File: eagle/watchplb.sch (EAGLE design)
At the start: 141 parts, among them IC1 SAM-M8Q, IC2 BM70BLES1FC2-0B03AA, Q1 8MHz / LFXTAL020423Reel, Q2 BC817-25SMD, Q3 DMN3023L-7, Q4 16MHz_LFXTAL051370Reel, U1 MCP111-XXXXX/TO, U2 STM32L073RZ, U3 MCP2200-I/SS, U4 TPD3E001DRLR

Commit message: added rf amp and sma connector, reorganised for better pdf page ordering
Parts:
- added U$2: RA07H4047M, Hick:RA07H4047M
- added X1: (no value), adafruit:SMACONNECTOR_EDGE
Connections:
- removed net N$38: C24.2, U$1.VDD_IO
- new net +12V: U$2.DRAIN_VOLTAGE
- new net RF_SIGNAL_AMPLIFIED: U$2.RF_OUT, X1.ANT
- net +3V3: now also C24.2, U$1.VDD_IO, U$2.GATE_VOLTAGE
- net GND: now also U$2.RF_GND_L, U$2.RF_GND_R, X1.GND1, X1.GND2, X1.GND3, X1.GND4
- net RF_SIGNAL: now also U$2.RF_IN
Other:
- moved on the sheet: 3V3, BTN_1, BTN_2, BTN_3, BTN_4, BTN_NRST, BT_RX, BT_TX, C1, C10, C11, C12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

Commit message: added battery protection circuit
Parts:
- added BAT: (no value), pinhead:PINHD-1X5
- added C38, C39, C40, C41, C44, C45, C46: 100nF, resistor:C-EUC0805
- added C42, C43: 1uF, resistor:C-EUC0805
- added D6: Zener 16V MMSZ5246BS-7-F, diode-1:DIODE-SOD323-R
- added D7: 100V, BAS16J,135, diode-1:DIODE-SOD323-R
- added D8, D9: (no value), adafruit:DIODESOD-123
- added IC3: LM1117DTX-ADJ-12V, lm1117:LM1117DTX-ADJ
- added IC4: LM1117DTX-ADJ-3V3, lm1117:LM1117DTX-ADJ
- added Q5, Q6: CSD18534Q5A, CSD18534Q5A:CSD18534Q5A
- added R30, R31, R32, R33, R34: 1k, resistor:R-EU_M0805
- added R35: 10k, resistor:R-EU_M0805
- added R36: 20mR, resistor:R-EU_M0805
- added R37, R38: 100R, resistor:R-EU_M0805
- added R39: 10M, resistor:R-EU_M0805
- added R40, R43: 5k1, resistor:R-EU_M0805
- added R41: 3M3, resistor:R-EU_M0805
- added R42: 1M, resistor:R-EU_M0805
- added R44: 470k, resistor:R-EU_M0805
- added SPARE_WAKEUP, SPARE_WAKEUP1: PTR1B2,54, testpad:PTR1B2,54
- added TR1: NTC 103AT, discrete:THERMISTOR_R-7,5
- added U5: BQ7790504, chips:BQ77904
- R10, R11, R14, R15, R18, R19, R20, R21, R22: value 220R -> 470R
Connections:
- removed net V+: D1.C, JP2.1
- new net BAT_PACK_GND: BAT.5, C38.2, C39.2, C40.2, C41.2, C42.1, C43.2, C44.1, C46.2, R36.2, R37.2, TR1.1, U5.AVSS, U5.CTRC, U5.CTRD, U5.DVSS
- new net BAT_PACK_NEG: D6.A, Q6.1, Q6.2, Q6.3, R41.1, R44.2
- new net BAT_PACK_POS: BAT.1, R30.1, R34.1
- new net N$38: R35.2, TR1.2, U5.TS
- new net N$46: D6.C, D7.C, Q6.4, R41.2, R42.1
- new net N$47: BAT.2, R31.1
- new net N$48: BAT.3, R32.1
- new net N$49: BAT.4, R33.1
- new net N$50: C39.1, R33.2, U5.VC1
- new net N$51: C40.1, R32.2, U5.VC2
- new net N$52: C41.1, R31.2, U5.VC3
- new net N$53: C38.1, R30.2, U5.VC4, U5.VC5
- new net N$54: C43.1, R34.2, U5.VDD
- new net N$55: Q5.1, Q5.2, Q5.3, R36.1, R38.2, R39.2
- new net N$56: C42.2, U5.AVDD, U5.CCFG
- new net N$57: C45.2, C46.1, R38.1, U5.SRN
- new net N$58: C44.2, C45.1, R37.1, U5.SRP
- new net N$59: Q5.5, Q5.6, Q5.7, Q5.8, Q6.5, Q6.6, Q6.7, Q6.8
- new net N$60: R35.1, U5.VTB
- new net N$62: Q5.4, R39.1, R40.1
- new net N$63: R40.2, U5.DSG
- new net N$64: D7.A, R42.2, R43.2
- new net N$65: R43.1, U5.CHG
- new net N$66: R44.1, U5.LD
- new net N$67: D8.A, SPARE_WAKEUP1.TP
- new net N$68: D9.A, SPARE_WAKEUP.TP
- net +3V3: now also D1.C, JP2.1
- net MCU_WAKEUP: now also D8.C, D9.C

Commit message: added calculations as excel file and battery charge circuitry in schematic
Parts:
- removed X1: (no value), adafruit:SMACONNECTOR_EDGE
- added C47, C49: 100nF, resistor:C-EUC0805
- added C48, C51, C52: 22uF 80-EDK226M050A9GAA, rcl:CPOL-EUE
- added C50: 4.7uF, resistor:C-EUC0805
- added D10: MBRS330T3, diode:MBRS330T3
- added J3: BNCPTH, SparkFun-Connectors:BNCPTH
- added J4: (no value), SparkFun-Connectors:USB_MICRO-B_FEMALE-SMT
- added L8: CTX10-4A-R, CTX10-4A-R:CTX10-4A-R
- added Q7: DMN3023L-7, transistor-small-signal:BSS123
- added R45: 330, resistor:R-EU_M0805
- added R46: 910R, resistor:R-EU_M0805
- added R47, R49: 10k, resistor:R-EU_M0805
- added R48: 330k, resistor:R-EU_M0805
- added R50: 0.25R, resistor:R-EU_M0805
- added R51: 120k, resistor:R-EU_M0805
- added R52: 12k4, resistor:R-EU_M0805
- added U$3: LT1513, Hick:LT1513
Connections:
- removed net BAT_PACK_NEG: D6.A, Q6.1, Q6.2, Q6.3, R41.1, R44.2
- new net N$61: C50.2, L8.2, U$3.VSW
- new net N$69: C48.+, J4.VBUS, L8.1, U$3.VIN
- new net N$70: L8.3, R49.2, R50.2
- new net N$71: C47.2, R45.2
- new net N$72: R45.1, U$3.VC
- new net N$73: Q7.D, R46.1
- new net N$74: R46.2, R47.2, R48.1
- new net N$75: C50.1, D10.A, L8.4
- new net N$76: C49.2, R48.2, R49.1, U$3.IFB
- new net N$77: R51.1, R52.2, U$3.VFB
- new net S/S: U$3.S/S
- net +3V3: now also R47.1
- net BAT_PACK_POS: now also C51.+, C52.+, D10.C, R51.2
- net GND: now also C47.1, C48.-, C49.1, C51.-, C52.-, D6.A, J3.GND, J4.GND, J4.SHIELD, Q6.1, Q6.2, Q6.3, Q7.S, R41.1, R44.2, R50.1, R52.1, U$3.GND; no longer X1.GND1, X1.GND2, X1.GND3, X1.GND4
- net RF_SIGNAL_AMPLIFIED: now also J3.OUT; no longer X1.ANT
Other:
- note added: "kabel mouser nr 601-606BBP wird ebenfalls benötigt"
- moved on the sheet: IC3, IC4

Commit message: added linear regulators + calculations for them, exported parts as library, generated new pdf
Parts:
- removed IC4: LM1117DTX-ADJ-3V3, lm1117:LM1117DTX-ADJ
- added B1, B2, B3, B4, B5, B6, B7: BLM18KG601SN1D, PCB4_Demoboard:B-EU_B0603
- added C53, C56, C59: 10uF 80-EDK106M025A9DAA, rcl:CPOL-EUE
- added C54, C57, C60: 100uF 647-GYA1E101MCQ1GS, rcl:CPOL-EUE
- added C55, C58, C61: NP, rcl:CPOL-EUE
- added IC5: LM1117DTX-ADJ-10V, lm1117:LM1117DTX-ADJ
- added IC6: LM1117DTX-ADJ-3V3, lm1117:LM1117DTX-ADJ
- added JP3: Power Disconnect, pinhead:PINHD-1X2
- added R53, R55, R57: 5k1, resistor:R-EU_M0805
- added R54, R56, R58: 47k, resistor:R-EU_M0805
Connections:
- new net 10V_INTERMEDIATE: C57.+, C59.+, IC5.OUT, IC6.IN, R55.1
- new net N$78: B4.2, CONFIG_INTERFACE_TEST_POINT.2
- new net N$79: B2.2, C1.1, C2.1, C3.1, IC1.VCC, IC1.VCC_IO, IC1.V_BCKP, R1.1, R2.1
- new net N$80: B3.2, IC2.VBAT, LED1.A, R3.1, U1.VSS
- new net N$81: B5.2, D1.C, JP2.1
- new net N$82: B6.2, C24.2, U$1.VDD_IO
- new net N$83: B7.2, U$2.GATE_VOLTAGE
- new net N$84: C53.+, C56.+, IC3.IN, IC5.IN, JP3.2
- new net N$85: C55.+, IC3.ADJ, R53.2, R54.1
- new net N$89: C58.+, IC5.ADJ, R55.2, R56.1
- new net N$92: C61.+, IC6.ADJ, R57.2, R58.1
- new net V+STM: B1.2, C10.2, C16.2, C4.1, C5.2, C6.2, C8.1, C9.1, U2.VDD, U2.VDDA, U2.VDD_2, U2.VDD_3, U2.VLCD
- net +12V: now also C54.+, IC3.OUT, R53.1
- net +3V3: now also B1.1, B2.1, B3.1, B4.1, B5.1, B6.1, B7.1, C60.+, IC6.OUT, R57.1; no longer C1.1, C10.2, C16.2, C2.1, C24.2, C3.1, C4.1, C5.2, C6.2, C8.1, C9.1, CONFIG_INTERFACE_TEST_POINT.2, D1.C, IC1.VCC, IC1.VCC_IO, IC1.V_BCKP, IC2.VBAT, JP2.1, LED1.A, R1.1, R2.1, R3.1, U$1.VDD_IO, U$2.GATE_VOLTAGE, U1.VSS, U2.VDD, U2.VDDA, U2.VDD_2, U2.VDD_3, U2.VLCD
- net BAT_PACK_POS: now also JP3.1
- net GND: now also C53.-, C54.-, C55.-, C56.-, C57.-, C58.-, C59.-, C60.-, C61.-, R54.2, R56.2, R58.2
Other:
- note added: "V+STM is 3V3 after ferrite"
- note removed: "Power Supply goes here"
- note removed: "ein/ausschalter direkt nach batterie"
- moved on the sheet: 3V3, BTN_1, BTN_2, BTN_3, BTN_4, BTN_NRST, C11, C12, C13, C17, C18, C21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

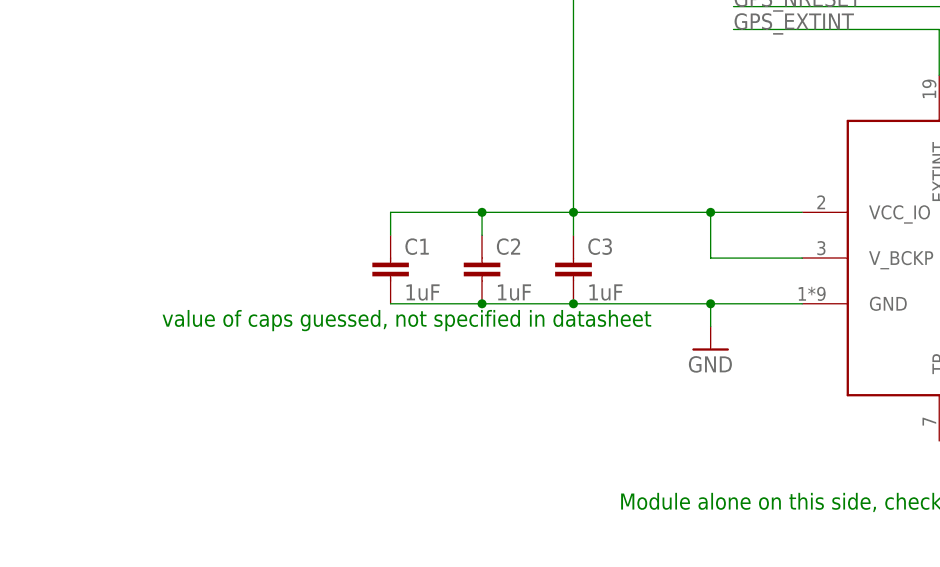
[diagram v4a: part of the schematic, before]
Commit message: added 4.7uF to gps module because the devboard does that.
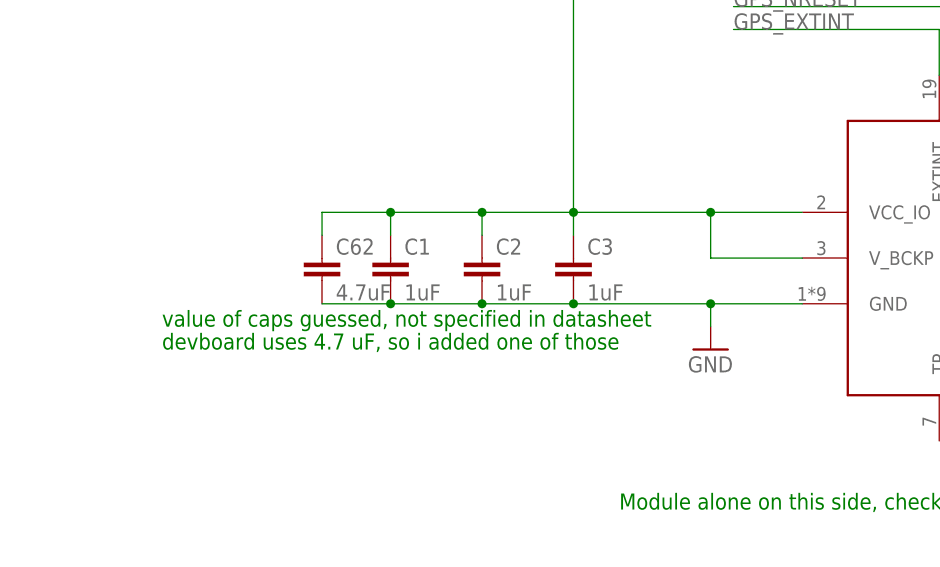
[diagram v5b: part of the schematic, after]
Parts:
- added C62: 4.7uF, resistor:C-EUC0805
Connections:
- net GND: now also C62.2
- net N$79: now also C62.1
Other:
- note added: "devboard uses 4.7 uF, so i added one of those"
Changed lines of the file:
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@@
 <part name="JP3" library="pinhead" deviceset="PINHD-1X2" device="" value="Power Disconnect"/>
 <part name="+3V3" library="supply1" deviceset="+3V3" device=""/>
+<part name="C62" library="resistor" deviceset="C-EU" device="C0805" value="4.7uF"/>
 </parts>
 <sheets>
@@
 <text x="937.26" y="307.34" size="1.778" layer="91">kabel mouser nr 601-606BBP wird ebenfalls benötigt</text>
 <text x="119.38" y="167.64" size="1.778" layer="91">V+STM is 3V3 after ferrite</text>
+<text x="586.74" y="81.28" size="1.778" layer="91">devboard uses 4.7 uF, so i added one of those</text>
 </plain>
 <instances>
@@
 <instance part="JP3" gate="G$1" x="292.1" y="358.14"/>
 <instance part="+3V3" gate="G$1" x="480.06" y="353.06"/>
+<instance part="C62" gate="G$1" x="604.52" y="91.44"/>
 </instances>
 <busses>
@@
 <wire x1="622.3" y1="86.36" x2="612.14" y2="86.36" width="0.1524" layer="91"/>
 <junction x="622.3" y="86.36"/>
+<pinref part="C62" gate="G$1" pin="2"/>
+<wire x1="612.14" y1="86.36" x2="604.52" y2="86.36" width="0.1524" layer="91"/>
+<junction x="612.14" y="86.36"/>
 </segment>
 <segment>
@@
 <wire x1="683.26" y1="124.46" x2="739.14" y2="124.46" width="0.1524" layer="91"/>
 <wire x1="739.14" y1="124.46" x2="739.14" y2="101.6" width="0.1524" layer="91"/>
-</segment>
-</net>
+<pinref part="C62" gate="G$1" pin="1"/>
+<wire x1="604.52" y1="93.98" x2="604.52" y2="96.52" width="0.1524" layer="91"/>
+<wire x1="604.52" y1="96.52" x2="612.14" y2="96.52" width="0.1524" layer="91"/>
+<junction x="612.14" y="96.52"/>
+</segment>
+</net>

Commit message: added missing names + new pdf
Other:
- note added: "AX5031"
- note added: "BQ7790504"
- note added: "RA07H4047M"
- note added: "SAM-M8Q"
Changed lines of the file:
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@@
 <text x="119.38" y="167.64" size="1.778" layer="91">V+STM is 3V3 after ferrite</text>
 <text x="586.74" y="81.28" size="1.778" layer="91">devboard uses 4.7 uF, so i added one of those</text>
+<text x="657.86" y="71.12" size="1.778" layer="91">SAM-M8Q</text>
+<text x="960.12" y="254" size="1.778" layer="91">AX5031</text>
+<text x="899.16" y="360.68" size="1.778" layer="91">RA07H4047M</text>
+<text x="116.84" y="299.72" size="1.778" layer="91">BQ7790504</text>
 </plain>
 <instances>
-<instance part="IC1" gate="G$1" x="662.94" y="76.2"/>
+<instance part="IC1" gate="G$1" x="662.94" y="76.2" smashed="yes"/>
 <instance part="+3V2" gate="G$1" x="683.26" y="142.24"/>
 <instance part="GND1" gate="1" x="647.7" y="81.28"/>
@@
 <instance part="C2" gate="G$1" x="622.3" y="91.44"/>
 <instance part="C3" gate="G$1" x="632.46" y="91.44"/>
-<instance part="IC2" gate="G$1" x="878.84" y="132.08"/>
+<instance part="IC2" gate="G$1" x="878.84" y="132.08" smashed="yes">
+<attribute name="NAME" x="918.21" y="139.7" size="1.778" layer="95" align="center-left"/>
+<attribute name="VALUE" x="885.19" y="139.7" size="1.778" layer="96" align="center-left"/>
+</instance>
 <instance part="GND2" gate="1" x="853.44" y="121.92"/>
 <instance part="+3V4" gate="G$1" x="866.14" y="162.56"/>
@@
 <instance part="+3V22" gate="G$1" x="396.24" y="81.28"/>
 <instance part="FRAME5" gate="G$1" x="553.72" y="193.04"/>
-<instance part="JP2" gate="G$1" x="764.54" y="279.4"/>
+<instance part="JP2" gate="G$1" x="764.54" y="279.4" smashed="yes">
+<attribute name="NAME" x="758.19" y="285.115" size="1.778" layer="95"/>
+<attribute name="VALUE" x="765.81" y="289.56" size="1.778" layer="96" rot="R180"/>
+</instance>
 <instance part="D1" gate="G$1" x="772.16" y="279.4" rot="R90"/>
 <instance part="GND25" gate="1" x="772.16" y="238.76"/>
@@
 </instance>
 <instance part="J3" gate="G$1" x="922.02" y="309.88" rot="MR0"/>
-<instance part="U$3" gate="G$1" x="381" y="256.54"/>
+<instance part="U$3" gate="G$1" x="381" y="256.54" smashed="yes"/>
 <instance part="GND34" gate="1" x="243.84" y="327.66"/>
 <instance part="L8" gate="A" x="375.92" y="271.78" rot="R90"/>
-<instance part="C48" gate="G$1" x="347.98" y="259.08"/>
+<instance part="C48" gate="G$1" x="347.98" y="259.08" smashed="yes">
+<attribute name="NAME" x="349.123" y="259.5626" size="1.778" layer="95"/>
+<attribute name="VALUE" x="349.377" y="266.2174" size="1.778" layer="96" rot="R180"/>
+</instance>
 <instance part="GND35" gate="1" x="381" y="218.44"/>
 <instance part="Q7" gate="G$1" x="340.36" y="231.14"/>
@@
 <instance part="R51" gate="G$1" x="429.26" y="254" rot="R90"/>
 <instance part="R52" gate="G$1" x="429.26" y="231.14" rot="R90"/>
-<instance part="C51" gate="G$1" x="439.42" y="243.84"/>
-<instance part="C52" gate="G$1" x="444.5" y="243.84"/>
+<instance part="C51" gate="G$1" x="439.42" y="243.84" smashed="yes">
+<attribute name="NAME" x="440.563" y="244.3226" size="1.778" layer="95"/>
+<attribute name="VALUE" x="440.563" y="236.7026" size="1.778" layer="96"/>
+</instance>
+<instance part="C52" gate="G$1" x="444.5" y="243.84" smashed="yes">
+<attribute name="NAME" x="445.643" y="244.3226" size="1.778" layer="95"/>
+<attribute name="VALUE" x="445.643" y="239.2426" size="1.778" layer="96"/>
+</instance>
 <instance part="D10" gate="G$1" x="421.64" y="261.62"/>
 <instance part="J4" gate="G$1" x="289.56" y="254"/>

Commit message: small schematic changes, started with layout
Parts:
- removed SPARE_WAKEUP, SPARE_WAKEUP1, USB_5V, USB_D+, USB_D-: PTR1B2,54, testpad:PTR1B2,54
- removed TR1: NTC 103AT, discrete:THERMISTOR_R-7,5
- added BAT_ADC, RF_SIGNAL: PTR1B2,54, testpad:PTR1B2,54
- added R59, R61: 10k, resistor:R-EU_M0805
- added R60: 47k, resistor:R-EU_M0805
- added R62: NTC 103AT, resistor:R-EU_M0805
- C38, C39, C40, C41, C42, C43, C44, C45, C46, C47, C49, C50, C62: device resistor:C-EUC0805 -> resistor:C-EUC0805K
- R36: device resistor:R-EU_M0805 -> resistor:R-EU_R2512
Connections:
- removed net S/S: U$3.S/S
- new net BAT_ADC: BAT_ADC.TP, R60.1, R61.2, U2.PA1
- new net CHARGER_CH_PRECH: Q7.G, U2.PD2
- new net CHARGER_SS: U$3.S/S, U2.PC12
- new net N$86: C11.2, R59.1
- net +3V3: now also R1.1, R2.1
- net +5V: no longer USB_5V.TP
- net BAT_PACK_GND: now also R62.2; no longer TR1.1
- net GND: now also R61.1
- net N$17: no longer USB_D-.TP
- net N$20: no longer USB_D+.TP
- net N$38: now also R62.1; no longer TR1.2
- net N$67: no longer SPARE_WAKEUP1.TP
- net N$68: no longer SPARE_WAKEUP.TP
- net N$79: no longer R1.1, R2.1
- net N$84: now also R60.2
- net NRST: now also R59.2; no longer C11.2
- net RF_SIGNAL: now also RF_SIGNAL.TP
- net USB_DATA_NEG: now also U4.IO1; no longer U4.IO2
- net USB_DATA_POS: now also U4.IO2; no longer U4.IO1
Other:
- moved on the sheet: Q7, R46, R47

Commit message: added some datasheets and continued with layout
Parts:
- removed C50: 4.7uF, resistor:C-EUC0805K
- removed VIBR: PTR1B2,54, testpad:PTR1B2,54
- added BAT_PACK_POS, USB_DN, USB_DP, USB_ID: PTR1B2,54, testpad:PTR1B2,54
- added C63: 4.7uF low esr 80-T521B475M35ATE150, rcl:CPOL-EUB/3528-21R
- R50: device resistor:R-EU_M0805 -> resistor:R-EU_R2512
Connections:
- net N$41 renamed ANT_N
- net N$44 renamed ANT_P
- removed net N$75: C50.1, D10.A, L8.4
- new net N$87: J4.ID, USB_ID.TP
- new net N$88: J4.D+, USB_DP.TP
- new net N$90: J4.D-, USB_DN.TP
- new net N$91: C63.-, D10.A, L8.3
- net BAT_PACK_POS: now also BAT_PACK_POS.TP
- net IND_LED_B: now also U2.PB0; no longer U2.PB1
- net IND_LED_G: now also U2.PC5; no longer U2.PB2
- net IND_LED_R: now also U2.PB2; no longer U2.PC5
- net IND_LED_W: now also U2.PB1; no longer U2.PB0
- net N$61: now also C63.+; no longer C50.2
- net N$70: now also L8.4; no longer L8.3
- net POW_LED_G2: now also U2.PA5; no longer U2.PA7
- net POW_LED_G3: now also U2.PA4; no longer U2.PC4
- net POW_LED_R: now also U2.PC4; no longer U2.PA4
- net POW_LED_Y: now also U2.PA7; no longer U2.PA5
- net VIBRATOR: no longer VIBR.TP
